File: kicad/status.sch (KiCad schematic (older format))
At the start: 34 parts, among them U45 74HC04, U46 74HC04

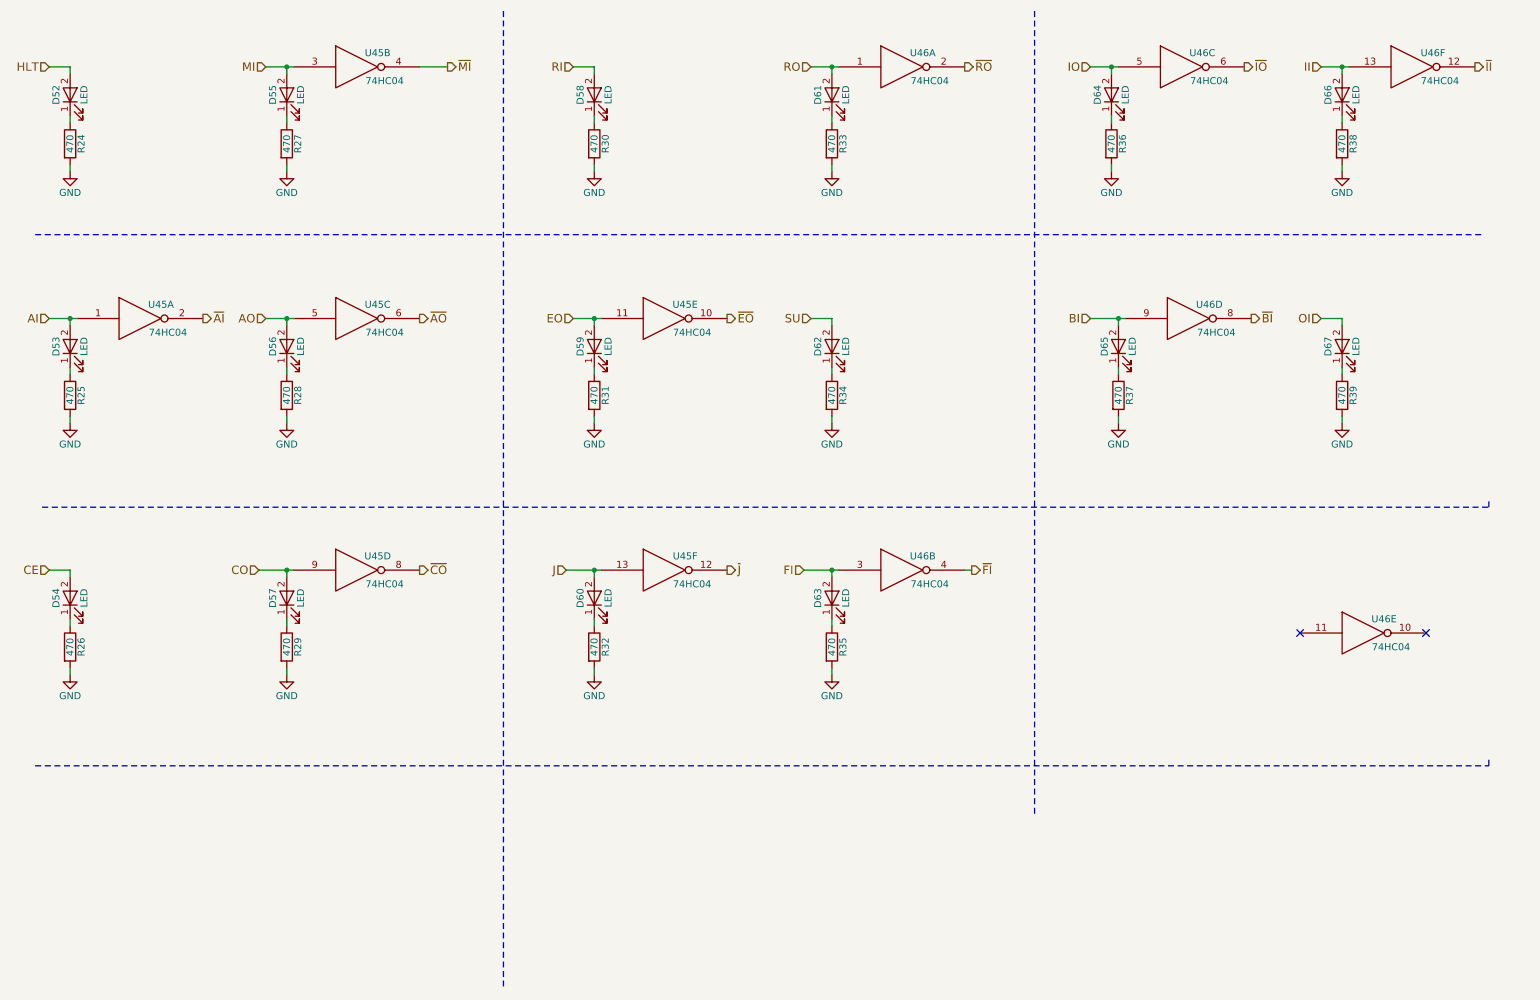
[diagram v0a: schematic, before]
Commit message: Update bugfix version to use updated kicad libraries
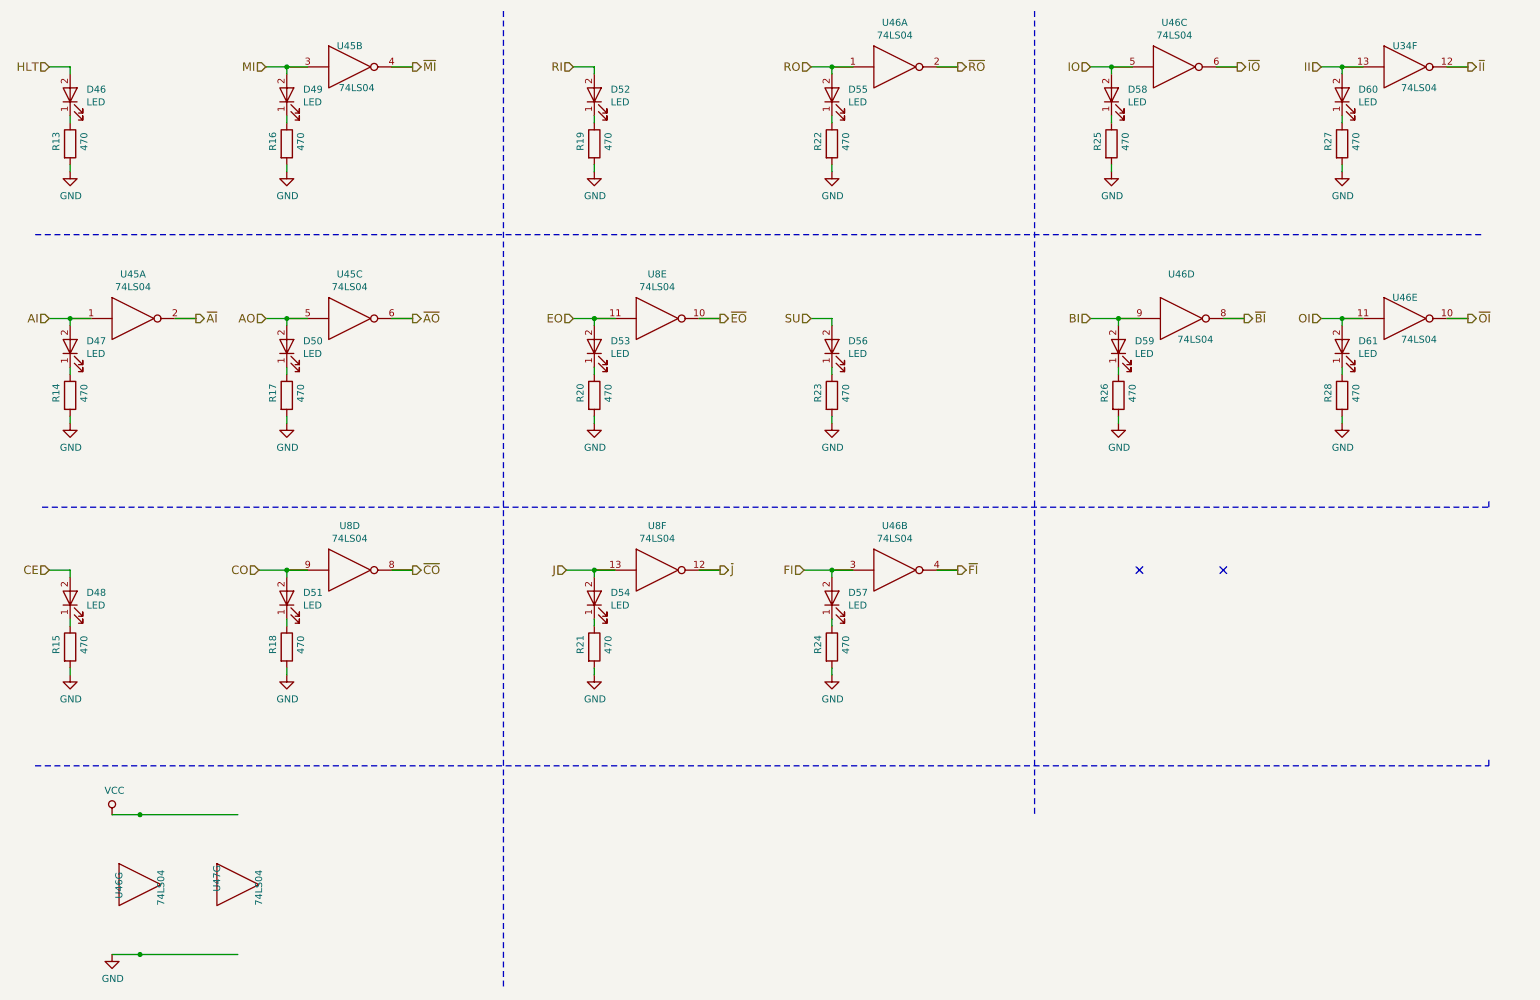
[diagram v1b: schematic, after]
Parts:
- removed D52, D53, D54, D55, D56, D57, D58, D59, D60, D61, D62, D63, D64, D65, D66, D67: LED, LEDs:LED-5MM, symbol LED
- removed R24, R25, R26, R27, R28, R29, R30, R31, R32, R33, R34, R35, R36, R37, R38, R39: 470, Resistors_THT:Resistor_Horizontal_RM7mm, symbol R
- removed U45, U46: 74HC04, Housings_DIP:DIP-14_W7.62mm_LongPads, symbol 74HC04
- added D46, D47, D48, D49, D50, D51, D52, D53, D54, D55, D56, D57, D58, D59, D60, D61: LED, symbol Device:LED
- added R13, R14, R15, R16, R17, R18, R19, R20, R21, R22, R23, R24, R25, R26, R27, R28: 470, symbol Device:R
- added U34, U45, U46, U47, U8: 74LS04, symbol 74xx:74LS04
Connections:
- net labels added: VCC, ~OI
- wire segments 66 -> 92
